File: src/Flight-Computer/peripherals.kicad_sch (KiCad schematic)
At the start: 29 parts, among them P3 USB, P4 282837-6, Q1 QS5U17TR, Q2 QS5U17TR, U10 RFM95W-868S2, U3 CP2102-GMR(QFN28), U4 SST25VF040B-50-4I-S2AE-T, U5 TS391IYLT, U6 TS391IYLT, U7 TS391IYLT

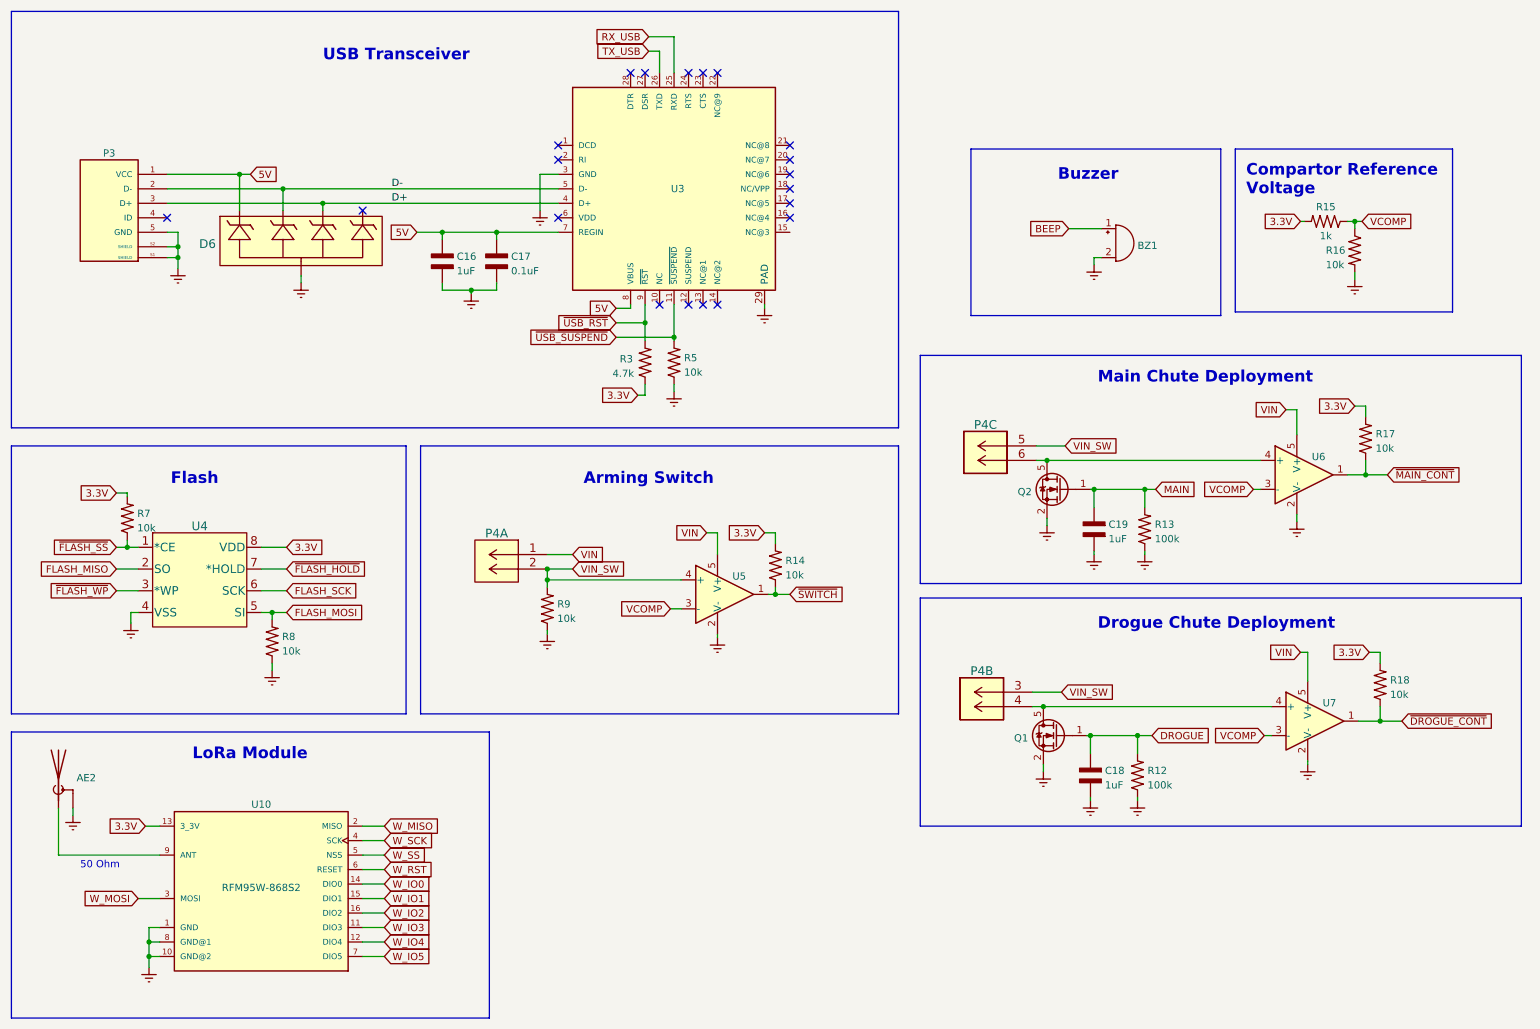
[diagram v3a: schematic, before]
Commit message: added decoupling capacitor to lora module
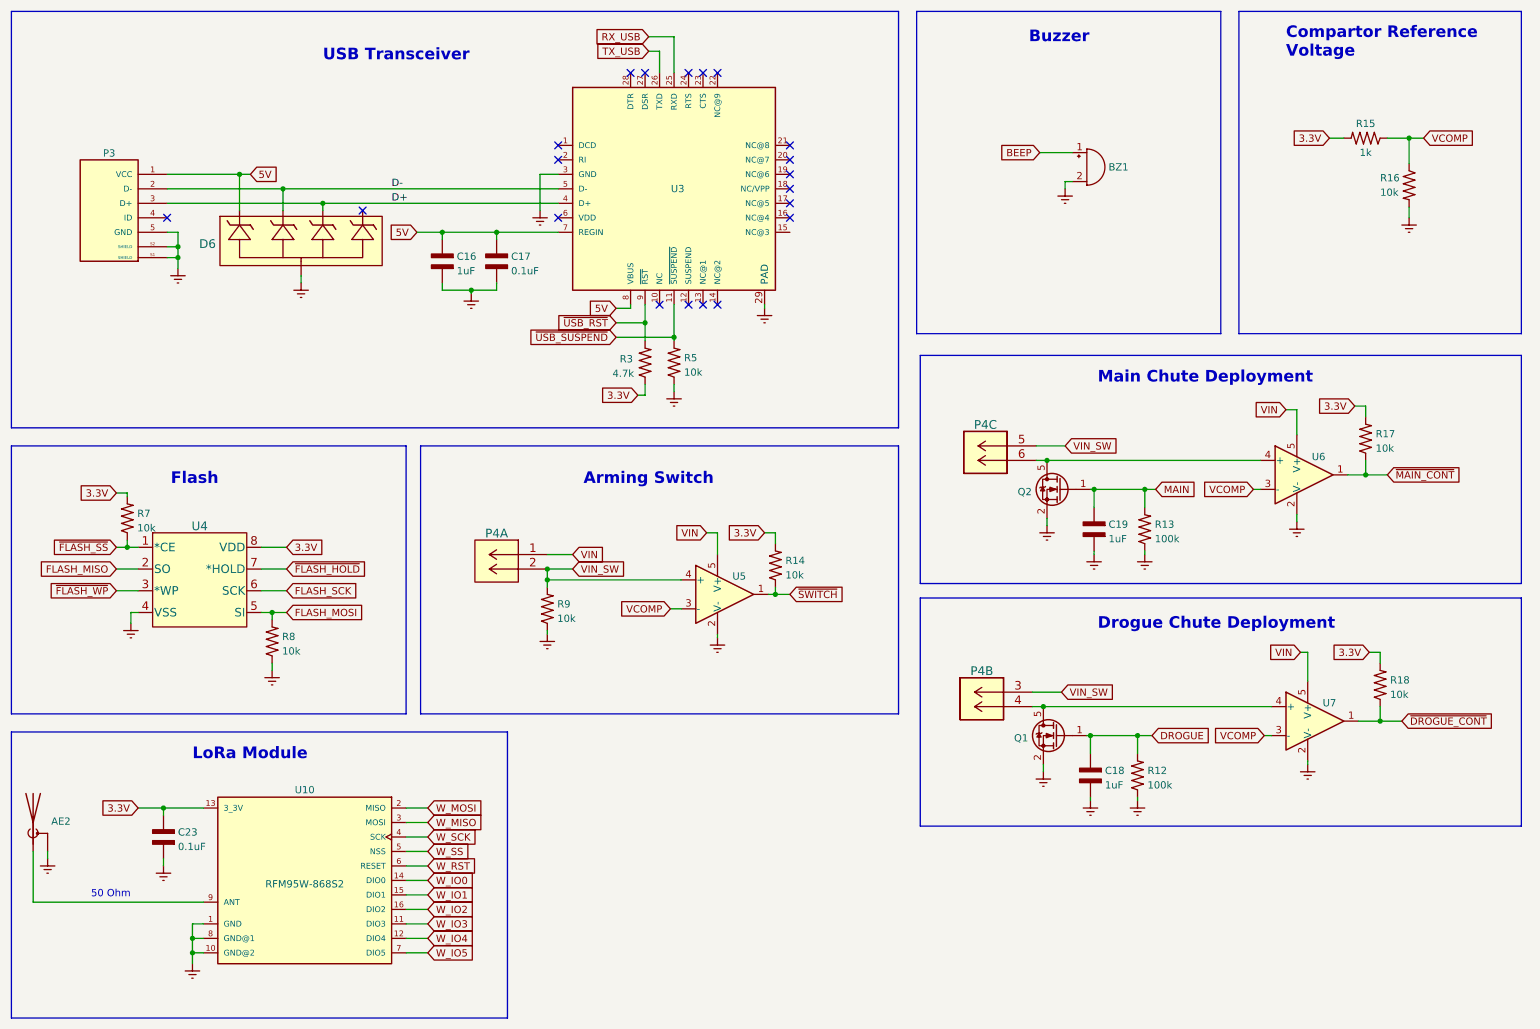
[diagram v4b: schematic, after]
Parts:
- added C23: 0.1uF, symbol Flight-Computer:CAP_0603
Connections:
- net 3.3V: now also C23.1
- net Earth: now also C23.2
- net W_MISO: now also U10.3 (MOSI); no longer U10.2 (MISO)
- net W_MOSI: now also U10.2 (MISO); no longer U10.3 (MOSI)
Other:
- moved on the sheet: AE2, BZ1, R15, R16, U10

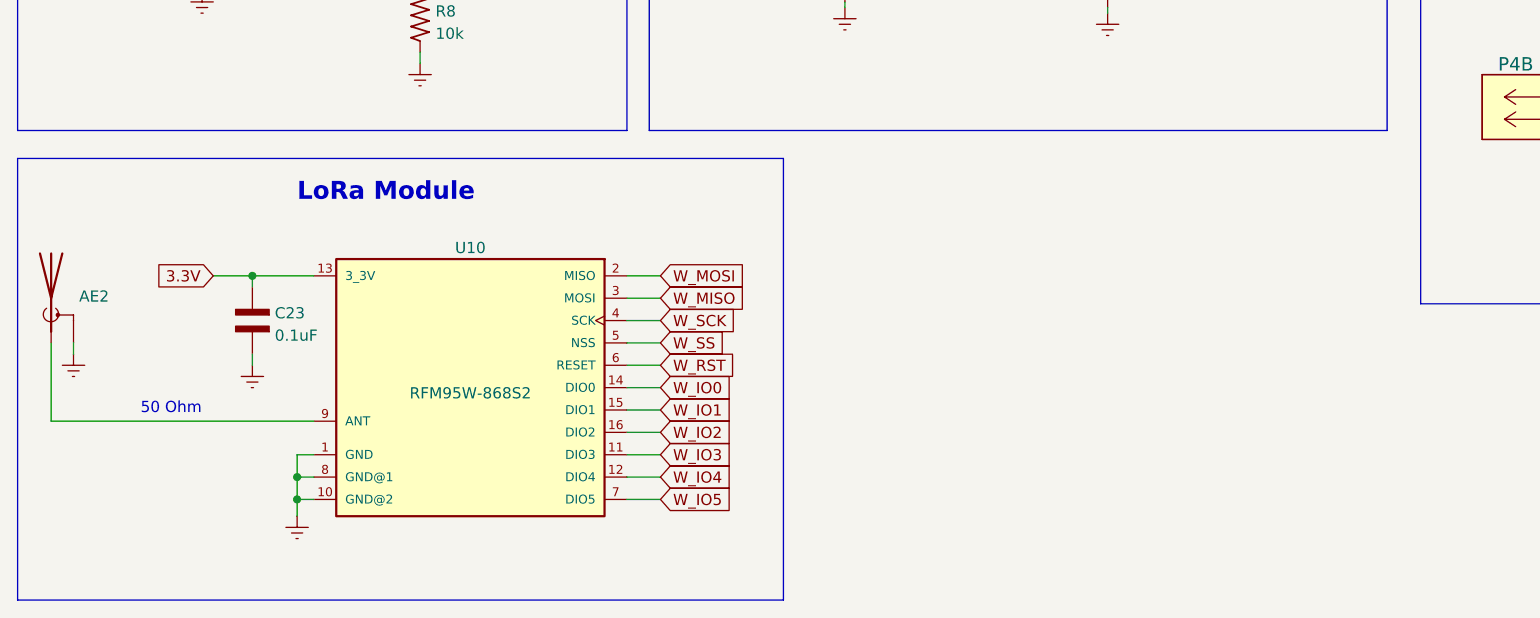
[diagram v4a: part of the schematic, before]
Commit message: minor schematic formatting changes
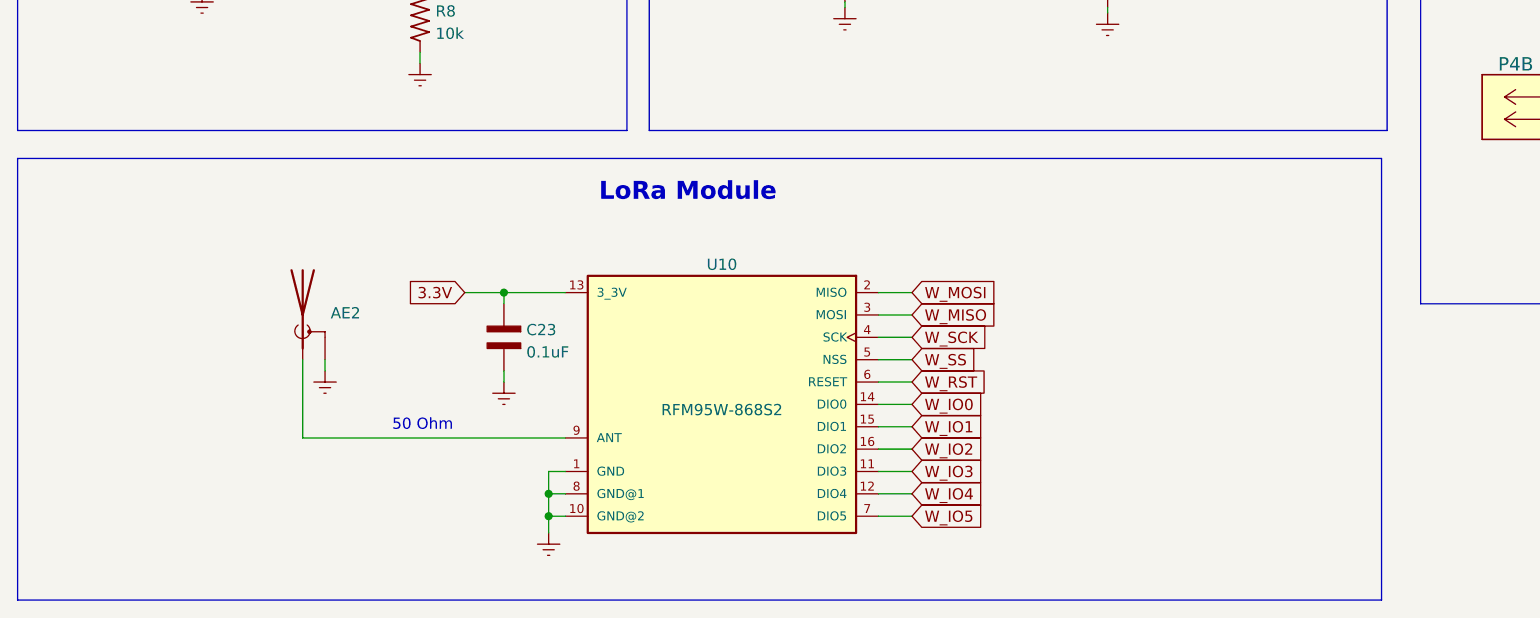
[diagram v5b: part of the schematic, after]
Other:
- moved on the sheet: AE2, C23, U10

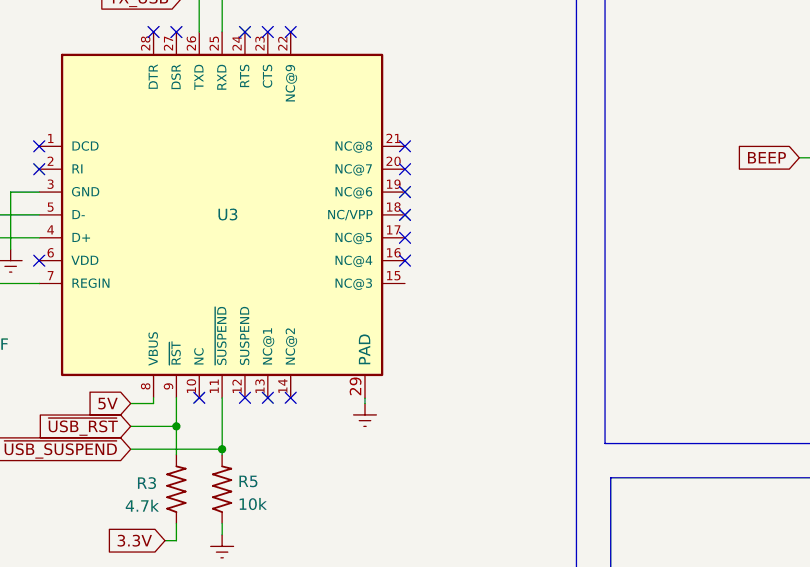
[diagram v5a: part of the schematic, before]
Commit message: added mcu signals for peripherals
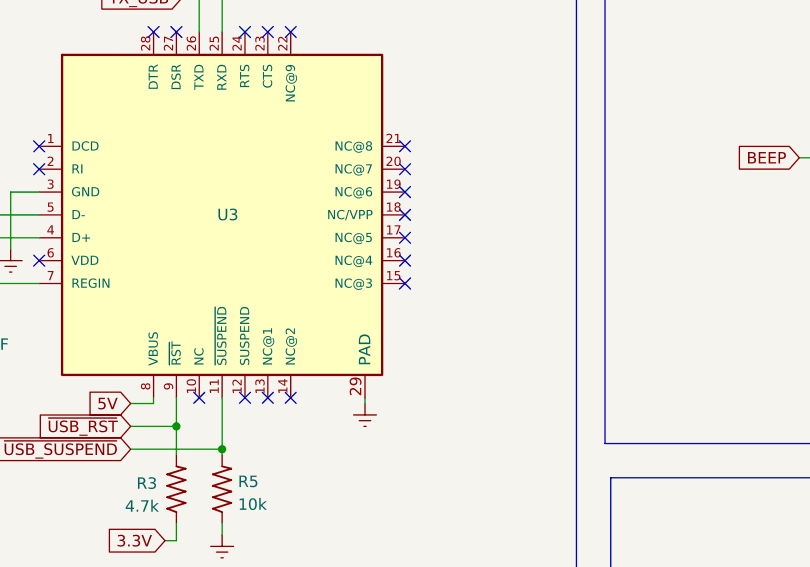
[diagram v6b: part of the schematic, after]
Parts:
- AE2: footprint (none) -> Flight-Computer:142-0701-851
- BZ1: footprint (none) -> Flight-Computer:AT-1438-TWT-R
- C16, C17, C18, C19, C23: footprint (none) -> Flight-Computer:CAP_0603
- D6: footprint SOD-123FL_MCC -> Flight-Computer:SP0504BAHTG
- P3: footprint BEL_SS-52300-001 -> Flight-Computer:10118194-0001LF
- P4: footprint 66953-005LF_AMP -> Flight-Computer:282837-6
- R12, R13, R14, R15, R16, R17, R18, R3, R5, R7, R8, R9: footprint (none) -> Flight-Computer:RES_0603
- U10: footprint XCVR_RFM95W-868S2 -> Flight-Computer:RFM95
- U3: footprint QFN28G_0.5-5X5MM -> Flight-Computer:CP2012-GMR
- U4: footprint SOIC8_S2A_SST_MCH -> Flight-Computer:SST25VF040B-50-4I-S2AE-T
- U5, U6, U7: footprint (none) -> Flight-Computer:TS391IYLT
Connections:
- no-connect marks 20 -> 21
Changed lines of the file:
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@@
   (junction (at 216.535 102.235) (diameter 0) (color 0 0 0 0)
   )
+  (no_connect (at 154.305 57.15))
   (no_connect (at 79.375 53.34))
   (no_connect (at 154.305 49.53))
@@
     (property "Reference" "U10" (id 0) (at 97.79 156.845 0))
     (property "Value" "RFM95W-868S2" (id 1) (at 97.79 173.355 0))
-    (property "Footprint" "XCVR_RFM95W-868S2" (id 2) (at 108.585 191.135 0)
+    (property "Footprint" "Flight-Computer:RFM95" (id 2) (at 108.585 191.135 0)
       (effects (font (size 1.27 1.27)) (justify left bottom) hide)
     )
@@
       (effects (font (size 1.524 1.524)) hide)
     )
-    (property "Footprint" "66953-005LF_AMP" (id 2) (at 107.95 144.145 0)
+    (property "Footprint" "Flight-Computer:282837-6" (id 2) (at 107.95 144.145 0)
       (effects (font (size 1.524 1.524)) hide)
     )
@@
       (effects (font (size 1.27 1.27)) hide)
     )
-    (property "Footprint" "" (id 2) (at 244.475 97.155 0)
+    (property "Footprint" "Flight-Computer:TS391IYLT" (id 2) (at 244.475 97.155 0)
       (effects (font (size 1.27 1.27)) hide)
     )
@@
       (effects (font (size 1.27 1.27)) (justify right))
     )
-    (property "Footprint" "" (id 2) (at 217.17 154.94 0)
+    (property "Footprint" "Flight-Computer:CAP_0603" (id 2) (at 217.17 154.94 0)
       (effects (font (size 1.27 1.27)) (justify left bottom) hide)
     )
@@
       (effects (font (size 1.27 1.27)) (justify right))
     )
-    (property "Footprint" "" (id 2) (at 113.03 64.77 0)
+    (property "Footprint" "Flight-Computer:CAP_0603" (id 2) (at 113.03 64.77 0)
       (effects (font (size 1.27 1.27)) (justify left bottom) hide)
     )
@@
       (effects (font (size 1.27 1.27)) (justify right))
     )
-    (property "Footprint" "" (id 2) (at 229.235 107.95 0)
+    (property "Footprint" "Flight-Computer:RES_0603" (id 2) (at 229.235 107.95 0)
       (effects (font (size 1.27 1.27)) (justify left bottom) hide)
     )
@@
       (effects (font (size 1.27 1.27)) (justify left) hide)
     )
-    (property "Footprint" "" (id 2) (at 205.74 43.18 90)
+    (property "Footprint" "Flight-Computer:AT-1438-TWT-R" (id 2) (at 205.74 43.18 90)
       (effects (font (size 1.27 1.27)) hide)
     )
@@
       (effects (font (size 1.27 1.27)) (justify right))
     )
-    (property "Footprint" "" (id 2) (at 146.685 78.74 0)
+    (property "Footprint" "Flight-Computer:RES_0603" (id 2) (at 146.685 78.74 0)
       (effects (font (size 1.27 1.27)) (justify left bottom) hide)
     )
@@
       (effects (font (size 1.27 1.27)) (justify right))
     )
-    (property "Footprint" "" (id 2) (at 103.505 64.77 0)
+    (property "Footprint" "Flight-Computer:CAP_0603" (id 2) (at 103.505 64.77 0)
       (effects (font (size 1.27 1.27)) (justify left bottom) hide)
     )
@@
       (effects (font (size 1.27 1.27)) (justify right))
     )
-    (property "Footprint" "" (id 2) (at 76.2 127.635 0)
+    (property "Footprint" "Flight-Computer:RES_0603" (id 2) (at 76.2 127.635 0)
       (effects (font (size 1.27 1.27)) (justify left bottom) hide)
     )
@@
     (property "Reference" "R15" (id 0) (at 255.27 38.1 0))
     (property "Value" "1k" (id 1) (at 255.27 43.18 0))
-    (property "Footprint" "" (id 2) (at 254 27.94 0)
+    (property "Footprint" "Flight-Computer:RES_0603" (id 2) (at 254 27.94 0)
       (effects (font (size 1.27 1.27)) (justify left bottom) hide)
     )
@@
       (effects (font (size 1.27 1.27)) (justify right))
     )
-    (property "Footprint" "" (id 2) (at 267.97 92.075 0)
+    (property "Footprint" "Flight-Computer:RES_0603" (id 2) (at 267.97 92.075 0)
       (effects (font (size 1.27 1.27)) (justify left bottom) hide)
     )
@@
       (effects (font (size 1.524 1.524)) hide)
     )
-    (property "Footprint" "66953-005LF_AMP" (id 2) (at 193.04 168.275 0)
+    (property "Footprint" "Flight-Computer:282837-6" (id 2) (at 193.04 168.275 0)
       (effects (font (size 1.524 1.524)) hide)
     )
@@
       (effects (font (size 1.27 1.27)) (justify right))
     )
-    (property "Footprint" "" (id 2) (at 124.46 121.92 0)
+    (property "Footprint" "Flight-Computer:RES_0603" (id 2) (at 124.46 121.92 0)
       (effects (font (size 1.27 1.27)) (justify left bottom) hide)
     )
@@
       (effects (font (size 1.524 1.524)) hide)
     )
-    (property "Footprint" "SOIC8_S2A_SST_MCH" (id 2) (at 51.435 132.715 0)
+    (property "Footprint" "Flight-Computer:SST25VF040B-50-4I-S2AE-T" (id 2) (at 51.435 132.715 0)
       (effects (font (size 1.524 1.524)) hide)
     )
@@
       (effects (font (size 1.27 1.27)) (justify right))
     )
-    (property "Footprint" "" (id 2) (at 83.185 167.64 0)
+    (property "Footprint" "Flight-Computer:CAP_0603" (id 2) (at 83.185 167.64 0)
       (effects (font (size 1.27 1.27)) (justify left bottom) hide)
     )
@@
       (effects (font (size 1.27 1.27)) (justify right))
     )
-    (property "Footprint" "" (id 2) (at 270.51 135.255 0)
+    (property "Footprint" "Flight-Computer:RES_0603" (id 2) (at 270.51 135.255 0)
       (effects (font (size 1.27 1.27)) (justify left bottom) hide)
     )
@@
       (effects (font (size 1.27 1.27)) (justify right))
     )
-    (property "Footprint" "" (id 2) (at 227.965 151.13 0)
+    (property "Footprint" "Flight-Computer:RES_0603" (id 2) (at 227.965 151.13 0)
       (effects (font (size 1.27 1.27)) (justify left bottom) hide)
     )
@@
       (effects (font (size 1.27 1.27)) (justify right))
     )
-    (property "Footprint" "" (id 2) (at 141.605 78.74 0)
+    (property "Footprint" "Flight-Computer:RES_0603" (id 2) (at 141.605 78.74 0)
       (effects (font (size 1.27 1.27)) (justify left bottom) hide)
     )
@@
       (effects (font (size 1.27 1.27)) (justify left bottom) hide)
     )
-    (property "Footprint" "QFN28G_0.5-5X5MM" (id 2) (at 98.425 76.2 0)
+    (property "Footprint" "Flight-Computer:CP2012-GMR" (id 2) (at 98.425 76.2 0)
       (effects (font (size 1.27 1.27)) (justify left bottom) hide)
     )
@@
       (effects (font (size 1.524 1.524)) hide)
     )
-    (property "Footprint" "66953-005LF_AMP" (id 2) (at 193.675 125.095 0)
+    (property "Footprint" "Flight-Computer:282837-6" (id 2) (at 193.675 125.095 0)
       (effects (font (size 1.524 1.524)) hide)
     )
@@
       (effects (font (size 1.27 1.27)) (justify right))
     )
-    (property "Footprint" "" (id 2) (at 164.465 114.3 0)
+    (property "Footprint" "Flight-Computer:RES_0603" (id 2) (at 164.465 114.3 0)
       (effects (font (size 1.27 1.27)) (justify left bottom) hide)
     )
@@
       (effects (font (size 1.27 1.27)) (justify right))
     )
-    (property "Footprint" "" (id 2) (at 217.805 111.76 0)
+    (property "Footprint" "Flight-Computer:CAP_0603" (id 2) (at 217.805 111.76 0)
       (effects (font (size 1.27 1.27)) (justify left bottom) hide)
     )
@@
       (effects (font (size 1.27 1.27)) hide)
     )
-    (property "Footprint" "" (id 2) (at 142.875 118.11 0)
+    (property "Footprint" "Flight-Computer:TS391IYLT" (id 2) (at 142.875 118.11 0)
       (effects (font (size 1.27 1.27)) hide)
     )
@@
       (effects (font (size 1.27 1.27)) (justify right) hide)
     )
-    (property "Footprint" "" (id 2) (at 50.165 160.02 0)
+    (property "Footprint" "Flight-Computer:142-0701-851" (id 2) (at 50.165 160.02 0)
       (effects (font (size 1.27 1.27)) hide)
     )
@@
       (effects (font (size 1.27 1.27)) (justify right))
     )
-    (property "Footprint" "" (id 2) (at 50.8 106.045 0)
+    (property "Footprint" "Flight-Computer:RES_0603" (id 2) (at 50.8 106.045 0)
       (effects (font (size 1.27 1.27)) (justify left bottom) hide)
     )
@@
       (effects (font (size 1.27 1.27)) (justify left bottom) hide)
     )
-    (property "Footprint" "BEL_SS-52300-001" (id 2) (at 43.815 69.85 0)
+    (property "Footprint" "Flight-Computer:10118194-0001LF" (id 2) (at 43.815 69.85 0)
       (effects (font (size 1.27 1.27)) (justify left bottom) hide)
     )
@@
       (effects (font (size 1.27 1.27)) hide)
     )
-    (property "Footprint" "" (id 2) (at 246.38 140.335 0)
+    (property "Footprint" "Flight-Computer:TS391IYLT" (id 2) (at 246.38 140.335 0)
       (effects (font (size 1.27 1.27)) hide)
     )
@@
       (effects (font (size 1.27 1.27)) (justify left))
     )
-    (property "Footprint" "" (id 2) (at 250.19 50.165 0)
+    (property "Footprint" "Flight-Computer:RES_0603" (id 2) (at 250.19 50.165 0)
       (effects (font (size 1.27 1.27)) (justify left bottom) hide)
     )
@@
       (effects (font (size 1.524 1.524)) hide)
     )
-    (property "Footprint" "SOD-123FL_MCC" (id 2) (at 47.752 79.375 0)
+    (property "Footprint" "Flight-Computer:SP0504BAHTG" (id 2) (at 47.752 79.375 0)
       (effects (font (size 1.524 1.524)) hide)
     )
